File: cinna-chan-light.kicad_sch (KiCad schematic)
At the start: 0 parts

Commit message: first commit!!!
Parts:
- added U3: ESP32-S3-WROOM-1, RF_Module:ESP32-S3-WROOM-1, symbol RF_Module:ESP32-S3-WROOM-1
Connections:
- new net: U3.1 (GND), U3.40 (GND), U3.41 (GND)
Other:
- sheet usbcpd ports: added COM_I2C_SCL, COM_I2C_SDA; removed none
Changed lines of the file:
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@@
 	(wire
 		(pts
-			(xy 175.26 133.35) (xy 179.07 133.35)
+			(xy 180.34 133.35) (xy 175.26 133.35)
 		)
 		(stroke
@@
 			"Pn9vc9snPhAEQRAEADBoCkEQBEEQBEGQXQfdDARBEARBEARBdhl0MxAEQRAEQRAE2WX+AAB//OMf"
 			"97oYCIIgCIIgCILsH3A3A0EQBEEQBEGQXQbdDARBEARBEARBdhl0MxAEQRAEQRAE2WX+f6pzsk0v"
-			"m9qYAAAAAElFTkSuQmCC"
+			"m9qYAAAAAElFTkSuQmCCbQAoAEYAbwBvAHQAbgBvAHQAZQBBAHIAZQBhACkAIgA+AA0ADQAKADwA"
+			"ZQBsAGUAbQBlAG4AdAANAA0ACgBiAGEAYwBrAGcAcgBvAHUAbgBkACAAIAAgACAAIAAgACAAIAAg"
+			"ACAAPQAgACIAdABoAGUAbQBlAGEAYgBsAGUAKABkAHQAYgAoAFQAYQBzAGsARABpAGEAbABvAGcA"
+			"LAAgADEANQAsACAAMAApACwAIAB0AGgAcgBlAGUAZABmAGEAYwBlACkAIgANAA0ACgBwAGEAZABk"
+			"AGkAbgBnACAAIAAgACAAIAAgACAAIAAgACAAIAAgACAAPQAgACIAdABoAGUAbQBlAGEAYgBsAGUA"
+			"KABnAHQAbQBhAHIAKABUAGEAcwBrAEQAaQBhAGwAbwBnACwAIAAxADUALAAgADAALAAgADMANgAw"
+			"ADIAKQAsAHIAZQBjAHQAKAAxADAAcgBwACwAMAAsADEAMAByAHAALAAwACkAKQAiAA0ADQAKAC8A"
+			"PgANAA0ACgA8AC8AaQBmAD4ADQANAAoAPABpAGYAIABpAGQAPQAiAGEAdABvAG0AKABGAG8AbwB0"
+			"AG4AbwB0AGUASQBjAG8AbgApACIAPgANAA0ACgA8AGUAbABlAG0AZQBuAHQADQANAAoAaABlAGkA"
+			"ZwBoAHQAIAAgACAAIAAgACAAIAAgACAAIAAgACAAIAAgAD0AIAAiAHMAeQBzAG0AZQB0AHIAaQBj"
+			"ACgANAA5ACkAIgANAA0ACgB3AGkAZAB0AGgAIAAgACAAIAAgACAAIAAgACAAIAAgACAAIAAgACAA"
+			"PQAgACIAcwB5AHMAbQBlAHQAcgBpAGMAKAA1ADAAKQAiAA0ADQAKAGEAYwBjAGUAcwBzAGkAYgBs"
+			"AGUAIAAgACAAIAAgACAAIAAgACAAIAA9ACAAIgB0AHIAdQBlACIADQANAAoAYQBjAGMAcgBvAGwA"
+			"ZQAgACAAIAAgACAAIAAgACAAIAAgACAAIAAgAD0AIAAiAGcAcgBhAHAAaABpAGMAIgANAA0ACgAv"
+			"AD4ADQANAAoAPAAvAGkAZgA+AA0ADQAKADwAaQBmACAAaQBkAD0AIgBhAHQAbwBtACgARgBvAG8A"
+			"dABuAG8AdABlAFQAZQB4AHQAKQAiAD4ADQANAAoAPABlAGwAZQBtAGUAbgB0AA0ADQAKAGYAbwBu"
+			"AHQAIAAgACAAIAAgACAAIAAgACAAIAAgACAAIAAgACAAIAA9ACAAIgBnAHQAZgAoAFQAYQBzAGsA"
+			"RABpAGEAbABvAGcAUwB0AHkAbABlACwAIAAxADUALAAgADAAKQAiAA0ADQAKAGYAbwByAGUAZwBy"
+			"AG8AdQBuAGQAIAAgAA=="
 		)
 	)
@@
 		)
 	)
+	(symbol
+		(lib_id "RF_Module:ESP32-S3-WROOM-1")
+		(at 49.53 113.03 0)
+		(unit 1)
+		(exclude_from_sim no)
+		(in_bom yes)
+		(on_board yes)
+		(dnp no)
+		(fields_autoplaced yes)
+		(property "Reference" "U3"
+			(at 51.6733 82.55 0)
+			(effects
+				(font
+					(size 1.27 1.27)
+				)
+				(justify left)
+			)
+		)
+		(property "Value" "ESP32-S3-WROOM-1"
+			(at 51.6733 85.09 0)
+			(effects
+				(font
+					(size 1.27 1.27)
+				)
+				(justify left)
+			)
+		)
+		(property "Footprint" "RF_Module:ESP32-S3-WROOM-1"
+			(at 49.53 110.49 0)
+			(effects
+				(font
+					(size 1.27 1.27)
+				)
+				(hide yes)
+			)
+		)
+		(property "Datasheet" "https://www.espressif.com/sites/default/files/documentation/esp32-s3-wroom-1_wroom-1u_datasheet_en.pdf"
+			(at 49.53 113.03 0)
+			(effects
+				(font
+					(size 1.27 1.27)
+				)
+				(hide yes)
+			)
+		)
+		(property "Description" "RF Module, ESP32-S3 SoC, Wi-Fi 802.11b/g/n, Bluetooth, BLE, 32-bit, 3.3V, onboard antenna, SMD"
+			(at 49.53 113.03 0)
+			(effects
+				(font
+					(size 1.27 1.27)
+				)
+				(hide yes)
+			)
+		)
+		(pin "4"
+		)
+		(pin "25"
+		)
+		(pin "29"
+		)
+		(pin "41"
+		)
+		(pin "40"
+		)
+		(pin "28"
+		)
+		(pin "14"
+		)
+		(pin "15"
+		)
+		(pin "36"
+		)
+		(pin "2"
+		)
+		(pin "6"
+		)
+		(pin "7"
+		)
+		(pin "35"
+		)
+		(pin "26"
+		)
+		(pin "19"
+		)
+		(pin "20"
+		)
+		(pin "30"
+		)
+		(pin "27"
+		)
+		(pin "39"
+		)
+		(pin "5"
+		)
+		(pin "3"
+		)
+		(pin "8"
+		)
+		(pin "1"
+		)
+		(pin "23"
+		)
+		(pin "31"
+		)
+		(pin "24"
+		)
+		(pin "12"
+		)
+		(pin "10"
+		)
+		(pin "38"
+		)
+		(pin "18"
+		)
+		(pin "13"
+		)
+		(pin "32"
+		)
+		(pin "33"
+		)
+		(pin "34"
+		)
+		(pin "16"
+		)
+		(pin "9"
+		)
+		(pin "17"
+		)
+		(pin "22"
+		)
+		(pin "37"
+		)
+		(pin "21"
+		)
+		(pin "11"
+		)
+		(instances
+			(project ""
+				(path "/eccd34c1-1a5c-4187-bee1-b0d1b475f777"
+					(reference "U3")
+					(unit 1)
+				)
+			)
+		)
+	)
 	(sheet
-		(at 179.07 121.92)
-		(size 88.9 30.48)
+		(at 180.34 121.92)
+		(size 102.87 30.48)
 		(exclude_from_sim no)
 		(in_bom yes)
@@
 		)
 		(property "Sheetname" "usbcpd"
-			(at 179.07 121.2084 0)
+			(at 180.34 121.2084 0)
 			(effects
 				(font
@@
 		)
 		(property "Sheetfile" "usbcpd.kicad_sch"
-			(at 179.07 152.9846 0)
+			(at 180.34 152.9846 0)
 			(effects
 				(font
@@
 		)
 		(pin "PP_USBC_VBUS" input
-			(at 179.07 130.81 180)
+			(at 180.34 130.81 180)
 			(effects
 				(font
@@
 		)
 		(pin "PP_3V3_MAIN" input
-			(at 179.07 133.35 180)
+			(at 180.34 133.35 180)
 			(effects
 				(font
@@
 			)
 		)
+		(pin "COM_I2C_SCL" input
+			(at 180.34 128.27 180)
+			(effects
+				(font
+					(size 1.27 1.27)
+				)
+				(justify left)
+			)
+		)
+		(pin "COM_I2C_SDA" input
+			(at 204.47 121.92 90)
+			(effects
+				(font
+					(size 1.27 1.27)
+				)
+				(justify right)
+			)
+		)

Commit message: added lcsc, datasheet, and footprint. couldn't find zener and polarized stuff tho
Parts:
- U3: LCSC (none) -> C2913192
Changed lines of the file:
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@@
 			"AAAAAAAAAAAAAAAAAAAAAAAAAAAAAAAAAAAAAAAAAAAAAAAAAAAAAAAAAAAAAAAAAAAAAAAAAAAA"
 			"AAAAAAAAAAAAAAAAAAAAAAAAAAAAAAAAAAAAAAAAAAAAAAAAAAAAAAAAAAAAAAAAAAAAAAAAAAAA"
-			"AAAAAAAAAAAAAAAAAA=="
+			"AAAAAAAAAAAAAAAAAAAAAAAAAAAAAAAAAAAAAAAAAAAAAAAAAAAAAAAAAAAAAAAAAAAAAAAAAAAA"
+			"AAAAAAAAAAAAAAAAAAAAAAAAAAAAAAAAAAAAAAAAAAAAAAAAAAAAAAAAAAAAAAAAAAAAAAAAAAAA"
+			"AAAAAAAAAAAAAAAAAAAAAAAAAAAAAAAAAAAAAAAAAAAAAAAAAAAAAAAAAAAAAAAAAAAAAAAAAAAA"
+			"AAAAAAAAAAAAAAAAAAAAAAAAAAAAAAAAAAAAAAAAAAAAAAAAAAAAAAAAAAAAAAAAAAAAAAAAAAAA"
+			"AAAAAAAAAAAAAAAAAAAAAAAAAAAAAAAAAAAAAAAAAAAAAAAAAAAAAAAAAAAAAAAAAAAAAAAAAAAA"
+			"AAAAAAAAAAAAAAAAAAAAAAAAAAAAAAAAAAAAAAAAAAAAAAAAAAAAAAAAAAAAAAAAAAAAAAAAAAAA"
+			"AAAAAAAAAAAAAAAAAAAAAAAAAAAAAAAAAAAAAAAAAAAAAAAAAAAAAAAAAAAAAAAAAAAAAAAAAAAA"
+			"AAAAAAAAAAAAAAAAAAAAAAAAAAAAAAAAAAAAAAAAAAAAAAAAAAAAAAAAAAAAAAAAAAAAAAAAAAAA"
+			"AAAAAAAAAAAAAAAAAAAAAAAAAAAAAAAAAAAAAAAAAAAAAAAAAAAAAAAAAAAAAAAAAAAAAAAAAAAA"
+			"AAAAAAAAAAAAAAAAAAAAAAAAAAAAAAAAAAAAAAAAAAAAAAAAAAAAAAAAAAAAAAAAAAAAAAAAAAAA"
+			"AAAAAAAAAAAAAAAAAAAAAAAAAAAAAAAAAAAAAAAAAAAAAAAAAAAAAAAAAAAAAAAAAAAAAAAAAAAA"
+			"AAAAAAAAAAAAAAAAAAAAAAAAAAAAAAAAAAAAAAAAAAAAAAAAAAAAAAAAAAAAAAAAAAAAAAAAAAAA"
+			"AAAAAAAAAAAAAAAAAAAAAAAAAAAAAAAAAAAAAAAAAAAAAAAAAAAAAAAAAAAAAAAAAAAAAAAAAAAA"
+			"AAAAAAAAAAAAAAAAAAAAAAAAAAAAAAAAAAAAAAAAAAAAAAAAAAAAAAAAAAAAAAAAAAAAAAAAAAAA"
+			"AAAAAAAAAAAAAAAAAAAAAAAAAAAAAAAAAAAAAAAAAAAAAAAAAAAAAAAAAAAAAAAAAAAAAAAAAAAA"
+			"AAAAAAAAAAAAAAAAAAAAAAAAAAAAAAAAAAAAAAAAAAAAAAAAAAAAAAAAAAAAAAAAAAAAAAAAAAAA"
+			"AAAAAAAAAAAAAAAAAAAAAAAAAAAAAAAAAAAAAAAAAAAAAAAAAAAAAAAAAAAAAAAAAAAAAAAAAAAA"
+			"AAAAAAAAAAAAAAAAAAAAAAAAAAAAAAAAAAAAAAAAAAAAAAAAAAAAAAAAAAAAAAAAAAAAAAAAAAAA"
+			"AAAAAAAAAAAAAAAAAAAAAAAAAAAAAAAAAAAAAAAAAAAAAAAAAAAAAAAAAAAAAAAAAAAAAAAAAAAA"
+			"AAAAAAAAAAAAAAAAAAAAAAAAAAAAAAAAAAAAAAAAAAAAAAAAAAAAAAAAAAAAAAAAAAAAAAAAAAAA"
+			"AAAAAAAAAAAAAAAAAAAAAAAAAAAAAAAAAAAAAAAAAAAAAAAAAAAAAAAAAAAAAAAAAAAAAAAAAAAA"
+			"AAAAAAAAAAAAAAAAAAAAAAAAAAAAAAAAAAAAAAAAAAAAAAAAAAAAAAAAAAAAAAAAAAAAAAAAAAAA"
+			"AAAAAAAAAAAAAAAAAAAAAAAAAAAAAAAAAAAAAAAAAAAAAAAAAAAAAAAAAAAAAAAAAAAAAAAAAAAA"
+			"AAAAAAAAAAAAAAAAAAAAAAAAAAAAAAAAAAAAAAAAAAAAAAAAAAAAAAAAAAAAAAAAAAAAAAAAAAAA"
+			"AAAAAAAAAAAAAAAAAAAAAAAAAAAAAAAAAAAAAAAAAAAAAAAAAAAAAAAAAAAAAAAAAAAAAAAAAAAA"
+			"AAAAAAAAAAAAAAAAAAAAAAAAAAAAAAAAAAAAAAAAAAAAAAAAAAAAAAAAAAAAAAAAAAAAAAAAAAAA"
+			"AAAAAAAAAAAAAAAAAAAAAAAAAAAAAAAAAAAAAAAAAAAAAAAAAAAAAAAAAAAAAAAAAAAAAAAAAAAA"
+			"AAAAAAAAAAAAAAAAAAAAAAAAAAAAAAAAAAAAAAAAAAAAAAAAAAAAAAAAAAAAAAAAAAAAAAAAAAAA"
+			"AAAAAAAAAAAAAAAAAAAAAAAAAAAAAAAAAAAAAAAAAAAAAAAAAAAAAAAAAAAAAAAAAAAAAAAAAAAA"
+			"AAAAAAAAAAAAAAAAAAAAAAAAAAAAAAAAAAAAAAAAAAAAAAAAAAAAAAAAAAAAAAAAAAAAAAAAAAAA"
+			"AAAAAAAAAAAAAAAAAAAAAAAAAAAAAAAAAAAAAAAAAAAAAAAAAAAAAAAAAAAAAAAAAAAAAAAAAAAA"
+			"AAAAAAAAAAAAAAAAAAAAAAAAAAAAAAAAAAAAAAAAAAAAAAAAAAAAAAAAAAAAAAAAAAAAAAAAAAAA"
+			"AAAAAAAAAAAAAAAAAAAAAAAAAAAAAAAAAAAAAAAAAAAAAAAAAAAAAAAAAAAAAAAAAAAAAAAAAAAA"
+			"AAAAAAAAAAAAAAAAAADlr2hYAAQAgPj/////////AMM4B+IBAAD4/////////wDnOAfiAQAA+P//"
+			"//////8AwTgH4gEAAPj/////////wOU4B+IBAAD4/////////8DqOAfiAQAA+P////////+AxDgH"
+			"4gEAAPj/////////ALg4B+IBAAD4/////////wDuOAfiAQAA+P////////+A8jgH4gEAAPj/////"
+			"////gME4B+IBAAD4/w=="
 		)
 	)
@@
 			(at 49.53 113.03 0)
 			(effects
+				(font
+					(size 1.27 1.27)
+				)
+				(hide yes)
+			)
+		)
+		(property "LCSC" "C2913192"
+			(at 49.53 113.03 0)
+			(effects

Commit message: Add light-white
Signed-off-by: sanyue <sanyue7th@gmail.com>
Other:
- added sheet light_white (light_white.kicad_sch)
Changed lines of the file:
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@@
 			"//////8AwTgH4gEAAPj/////////wOU4B+IBAAD4/////////8DqOAfiAQAA+P////////+AxDgH"
 			"4gEAAPj/////////ALg4B+IBAAD4/////////wDuOAfiAQAA+P////////+A8jgH4gEAAPj/////"
-			"////gME4B+IBAAD4/w=="
+			"////gME4B+IBAAD4/wAAAAAAAAAAAAAAAAAAAAAAAAAAAAAAAAAAAAAAAAAAAAAAAAAAAAAAAAAA"
+			"AAAAAAAAAAAAAAAAAAAAAAAAAAAAAAAAAAAAAAAAAAAAAAAAAAAAAAAAAAAAAAAAAAAAAAAAAAAA"
+			"AAAAAAAAAAAAAAAAAAAAAAAAAAAAAAAAAAAAAAAAAAAAAAAAAAAAAAAAAAAAAAAAAAAAAAAAAAAA"
+			"AAAAAAAAAAAAAAAAAAAAAAAAAAAAAAAAAAAAAAAAAAAAAAAAAAAAAAAAAAAAAAAAAAAAAAAAAAAA"
+			"AAAAAAAAAAAAAAAAAAAAAAAAAAAAAAAAAAAAAAAAAAAAAAAAAAAAAAAAAAAAAAAAAAAAAAAAAAAA"
+			"AAAAAAAAAAAAAAAAAAAAAAAAAAAAAAAAAAAAAAAAAAAAAAAAAAAAAAAAAAAAAAAAAAAAAAAAAAAA"
+			"AAAAAAAAAAAAAAAAAAAAAAAAAAAAAAAAAAAAAAAAAAAAAAAAAAAAAAAAAAAAAAAAAAAAAAAAAAAA"
+			"AAAAAAAAAAAAAAAAAAAAAAAAAAAAAAAAAAAAAAAAAAAAAAAAAAAAAAAAAAAAAAAAAAAAAAAAAAAA"
+			"AAAAAAAAAAAAAAAAAAAAAAAAAAAAAAAAAAAAAAAAAAAAAAAAAAAAAAAAAAAAAAAAAAAAAAAAAAAA"
+			"AAAAAAAAAAAAAAAAAAAAAAAAAAAAAAAAAAAAAAAAAAAAAAAAAAAAAAAAAAAAAAAAAAAAAAAAAAAA"
+			"AAAAAAAAAAAAAAAAAAAAAAAAAAAAAAAAAAAAAAAAAAAAAAAAAAAAAAAAAAAAAAAAAAAAAAAAAAAA"
+			"AAAAAAAAAAAAAAAAAAAAAAAAAAAAAAAAAAAAAAAAAAAAAAAAAAAAAAAAAAAAAAAAAAAAAAAAAAAA"
+			"AAAAAAAAAAAAAAAAAAAAAAAAAAAAAAAAAAAAAAAAAAAAAAAAAAAAAAAAAAAAAAAAAAAAAAAAAAAA"
+			"AAAAAAAAAAAAAAAAAAAAAAAAAAAAAAAAAAAAAAAAAAAAAAAAAAAAAAAAAAAAAAAAAAAAAAAAAAAA"
+			"AAAAAAAAAAAAAAAAAAAAAAAAAAAAAAAAAAAAAAAAAAAAAAAAAAAAAAAAAAAAAAAAAAAAAAAAAAAA"
+			"AAAAAAAAAAAAAAAAAAAAAAAAAAAAAAAAAAAAAAAAAAAAAAAAAAAAAAAAAAAAAAAAAAAAAAAAAAAA"
+			"AAAAAAAAAAAAAAAAAAAAAAAAAAAAAAAAAAAAAAAAAAAAAAAAAAAAAAAAAAAAAAAAAAAAAAAAAAAA"
+			"AAAAAAAAAAAAAAAAAAAAAAAAAAAAAAAAAAAAAAAAAAAAAAAAAAAAAAAAAAAAAAAAAAAAAAAAAAAA"
+			"AAAAAAAAAAAAAAAAAA=="
 		)
 	)
@@
 				)
 			)
+		)
+	)
+	(sheet
+		(at 157.48 33.02)
+		(size 81.28 20.32)
+		(exclude_from_sim no)
+		(in_bom yes)
+		(on_board yes)
+		(dnp no)
+		(fields_autoplaced yes)
+		(stroke
+			(width 0.1524)
+			(type solid)
+		)
+		(fill
+			(color 0 0 0 0.0000)
+		)
+		(property "Sheetname" "light_white"
+			(at 157.48 32.3084 0)
+			(effects
+				(font
+					(size 1.27 1.27)
+				)
+				(justify left bottom)
+			)
+		)
+		(property "Sheetfile" "light_white.kicad_sch"
+			(at 157.48 53.9246 0)
+			(effects
+				(font
+					(size 1.27 1.27)
+				)
+				(justify left top)
+			)
+		)
+		(instances
+			(project "cinna-chan-light"
+				(path "/eccd34c1-1a5c-4187-bee1-b0d1b475f777"
+					(page "4")
+				)
+			)

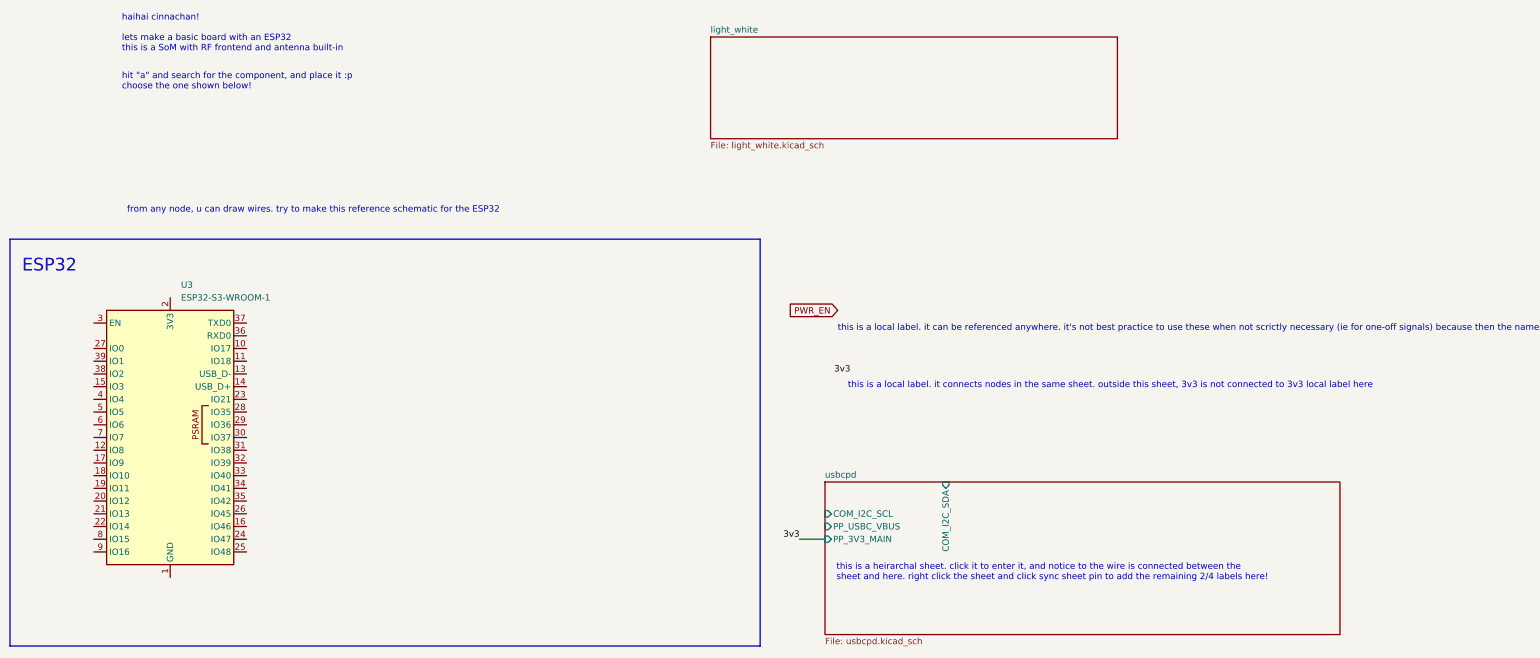
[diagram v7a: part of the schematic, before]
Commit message: Cleanup, add 5vREG block
Signed-off-by: sanyue <sanyue7th@gmail.com>
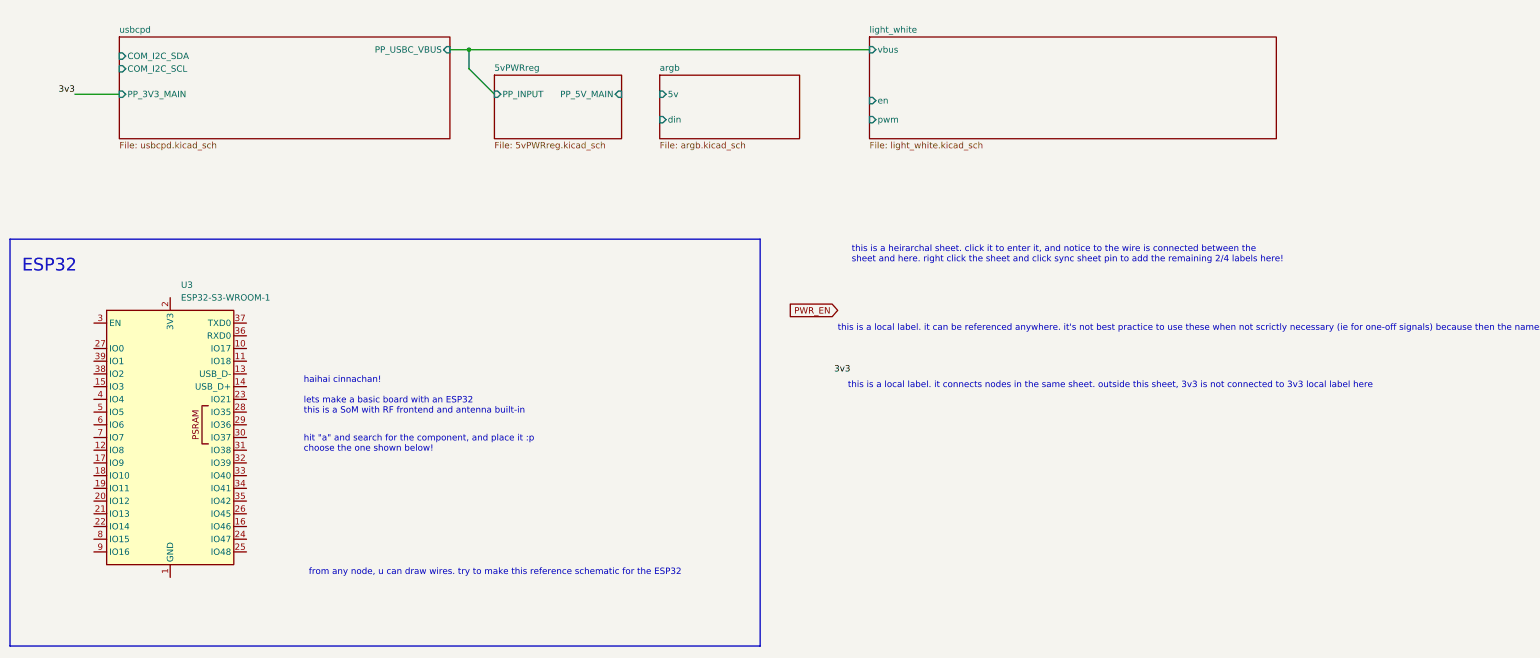
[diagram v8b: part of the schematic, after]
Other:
- added sheet 5vPWRreg (5vPWRreg.kicad_sch)
- added sheet argb (argb.kicad_sch)
- sheet light_white ports: added en, pwm, vbus; removed none
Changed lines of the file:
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@@
 	(text "haihai cinnachan!\n\nlets make a basic board with an ESP32\nthis is a SoM with RF frontend and antenna built-in"
 		(exclude_from_sim no)
-		(at 39.878 32.258 0)
+		(at 76.2 104.648 0)
 		(effects
 			(font
@@
 	(text "hit \"a\" and search for the component, and place it :p\nchoose the one shown below!"
 		(exclude_from_sim no)
-		(at 39.878 41.91 0)
+		(at 76.2 114.3 0)
 		(effects
 			(font
@@
 	(text "this is a heirarchal sheet. click it to enter it, and notice to the wire is connected between the \nsheet and here. right click the sheet and click sync sheet pin to add the remaining 2/4 labels here!"
 		(exclude_from_sim no)
-		(at 182.626 139.954 0)
+		(at 185.674 76.454 0)
 		(effects
 			(font
@@
 	(text "from any node, u can draw wires. try to make this reference schematic for the ESP32"
 		(exclude_from_sim no)
-		(at 40.894 67.564 0)
+		(at 77.216 139.954 0)
 		(effects
 			(font
@@
 		)
 	)
+	(junction
+		(at 109.22 35.56)
+		(diameter 0)
+		(color 0 0 0 0)
+	)
 	(wire
 		(pts
-			(xy 180.34 133.35) (xy 175.26 133.35)
+			(xy 109.22 35.56) (xy 189.23 35.56)
 		)
 		(stroke
@@
 		)
 	)
+	(wire
+		(pts
+			(xy 105.41 35.56) (xy 109.22 35.56)
+		)
+		(stroke
+			(width 0)
+			(type default)
+		)
+	)
+	(wire
+		(pts
+			(xy 109.22 39.37) (xy 114.3 44.45)
+		)
+		(stroke
+			(width 0)
+			(type default)
+		)
+	)
+	(wire
+		(pts
+			(xy 39.37 44.45) (xy 30.48 44.45)
+		)
+		(stroke
+			(width 0)
+			(type default)
+		)
+	)
+	(wire
+		(pts
+			(xy 109.22 39.37) (xy 109.22 35.56)
+		)
+		(stroke
+			(width 0)
+			(type default)
+		)
+	)
 	(image
-		(at 63.5 53.34)
+		(at 99.822 125.73)
 		(scale 0.160512)
 		(data "iVBORw0KGgoAAAANSUhEUgAABCIAAAGQCAIAAAD0iVbdAAAAA3NCSVQICAjb4U/gAAAACXBIWXMA"
@@
 			"AAAAAAAAAAAAAAAAAAAAAAAAAAAAAAAAAAAAAAAAAAAAAAAAAAAAAAAAAAAAAAAAAAAAAAAAAAAA"
 			"AAAAAAAAAAAAAAAAAAAAAAAAAAAAAAAAAAAAAAAAAAAAAAAAAAAAAAAAAAAAAAAAAAAAAAAAAAAA"
+			"AAAAAAAAAAAAAAAAAAAAAAAAAAAAAAAAAAAAAAAAAAAAAAAAAAAAAAAAAAAAAAAAAAAAAAAAAAAA"
+			"AAAAAAAAAAAAAAAAAAAAAAAAAAAAAAAAAAAAAAAAAAAAAAAAAAAAAAAAAAAAAAAAAAAAAAAAAAAA"
+			"AAAAAAAAAAAAAAAAAAAAAAAAAAAAAAAAAAAAAAAAAAAAAAAAAAAAAAAAAAAAAAAAAAAAAAAAAAAA"
+			"AAAAAAAAAAAAAAAAAAAAAAAAAAAAAAAAAAAAAAAAAAAAAAAAAAAAAAAAAAAAAAAAAAAAAAAAAAAA"
+			"AAAAAAAAAAAAAAAAAAAAAAAAAAAAAAAAAAAAAAAAAAAAAAAAAAAAAAAAAAAAAAAAAAAAAAAAAAAA"
+			"AAAAAAAAAAAAAAAAAAAAAAAAAAAAAAAAAAAAAAAAAAAAAAAAAAAAAAAAAAAAAAAAAAAAAAAAAAAA"
+			"AAAAAAAAAAAAAAAAAAAAAAAAAAAAAAAAAAAAAAAAAAAAAAAAAAAAAAAAAAAAAAAAAAAAAAAAAAAA"
+			"AAAAAAAAAAAAAAAAAAAAAAAAAAAAAAAAAAAAAAAAAAAAAAAAAAAAAAAAAAAAAAAAAAAAAAAAAAAA"
+			"AAAAAAAAAAAAAAAAAAAAAAAAAAAAAAAAAAAAAAAAAAAAAAAAAAAAAAAAAAAAAAAAAAAAAAAAAAAA"
+			"AAAAAAAAAAAAAAAAAAAAAAAAAAAAAAAAAAAAAAAAAAAAAAAAAAAAAAAAAAAAAAAAAAAAAAAAAAAA"
+			"AAAAAAAAAAAAAAAAAAAAAAAAAAAAAAAAAAAAAAAAAAAAAAAAAAAAAAAAAAAAAAAAAAAAAAAAAAAA"
+			"AAAAAAAAAAAAAAAAAAAAAAAAAAAAAAAAAAAAAAAAAAAAAAAAAAAAAAAAAAAAAAAAAAAAAAAAAAAA"
+			"AAAAAAAAAAAAAAAAAAAAAAAAAAAAAAAAAAAAAAAAAAAAAAAAAAAAAAAAAAAAAAAAAAAAAAAAAAAA"
+			"AAAAAAAAAAAAAAAAAAAAAAAAAAAAAAAAAAAAAAAAAAAAAAAAAAAAAAAAAAAAAAAAAAAAAAAAAAAA"
+			"AAAAAAAAAAAAAAAAAAAAAAAAAAAAAAAAAAAAAAAAAAAAAAAAAAAAAAAAAAAAAAAAAAAAAAAAAAAA"
+			"AAAAAAAAAAAAAAAAAAAAAAAAAAAAAAAAAAAAAAAAAAAAAAAAAAAAAAAAAAAAAAAAAAAAAAAAAAAA"
+			"AAAAAAAAAAAAAAAAAAAAAAAAAAAAAAAAAAAAAAAAAAAAAAAAAAAAAAAAAAAAAAAAAAAAAAAAAAAA"
+			"AAAAAAAAAAAAAAAAAAAAAAAAAAAAAAAAAAAAAAAAAAAAAAAAAAAAAAAAAAAAAAAAAAAAAAAAAAAA"
 			"AAAAAAAAAAAAAAAAAA=="
 		)
 	)
 	(label "3v3"
-		(at 175.26 133.35 180)
+		(at 30.48 44.45 180)
 		(effects
 			(font
@@
 	)
 	(sheet
-		(at 157.48 33.02)
+		(at 114.3 40.64)
+		(size 25.4 12.7)
+		(exclude_from_sim no)
+		(in_bom yes)
+		(on_board yes)
+		(dnp no)
+		(fields_autoplaced yes)
+		(stroke
+			(width 0.1524)
+			(type solid)
+		)
+		(fill
+			(color 0 0 0 0.0000)
+		)
+		(property "Sheetname" "5vPWRreg"
+			(at 114.3 39.9284 0)
+			(effects
+				(font
+					(size 1.27 1.27)
+				)
+				(justify left bottom)
+			)
+		)
+		(property "Sheetfile" "5vPWRreg.kicad_sch"
+			(at 114.3 53.9246 0)
+			(effects
+				(font
+					(size 1.27 1.27)
+				)
+				(justify left top)
+			)
+		)
+		(pin "PP_INPUT" input
+			(at 114.3 44.45 180)
+			(effects
+				(font
+					(size 1.27 1.27)
+				)
+				(justify left)
+			)
+		)
+		(pin "PP_5V_MAIN" input
+			(at 139.7 44.45 0)
+			(effects
+				(font
+					(size 1.27 1.27)
+				)
+				(justify right)
+			)
+		)
+		(instances
+			(project "cinna-chan-light"
+				(path "/eccd34c1-1a5c-4187-bee1-b0d1b475f777"
+					(page "5")
+				)
+			)
+		)
+	)
+	(sheet
+		(at 189.23 33.02)
 		(size 81.28 20.32)
 		(exclude_from_sim no)
@@
 		)
 		(property "Sheetname" "light_white"
-			(at 157.48 32.3084 0)
+			(at 189.23 32.3084 0)
 			(effects
 				(font
@@
 		)
 		(property "Sheetfile" "light_white.kicad_sch"
-			(at 157.48 53.9246 0)
+			(at 189.23 53.9246 0)
 			(effects
 				(font
@@
 				)
 				(justify left top)
+			)
+		)
+		(pin "en" input
+			(at 189.23 45.72 180)
+			(effects
+				(font
+					(size 1.27 1.27)
+				)
+				(justify left)
+			)
+		)
+		(pin "vbus" input
+			(at 189.23 35.56 180)
+			(effects
+				(font
+					(size 1.27 1.27)
+				)
+				(justify left)
+			)
+		)
+		(pin "pwm" input
+			(at 189.23 49.53 180)
+			(effects
+				(font
+					(size 1.27 1.27)
+				)
+				(justify left)
 			)
 		)
@@
 	)
 	(sheet
-		(at 180.34 121.92)
-		(size 102.87 30.48)
+		(at 147.32 40.64)
+		(size 27.94 12.7)
 		(exclude_from_sim no)
 		(in_bom yes)
@@
 			(color 0 0 0 0.0000)
 		)
+		(property "Sheetname" "argb"
+			(at 147.32 39.9284 0)
+			(effects
+				(font
+					(size 1.27 1.27)
+				)
+				(justify left bottom)
+			)
+		)
+		(property "Sheetfile" "argb.kicad_sch"
+			(at 147.32 53.9246 0)
+			(effects
+				(font
+					(size 1.27 1.27)
+				)
+				(justify left top)
+			)
+		)
+		(pin "din" input
+			(at 147.32 49.53 180)
+			(effects
+				(font
+					(size 1.27 1.27)
+				)
+				(justify left)
+			)
+		)
+		(pin "5v" input
+			(at 147.32 44.45 180)
+			(effects
+				(font
+					(size 1.27 1.27)
+				)
+				(justify left)
+			)
+		)
+		(instances
+			(project "cinna-chan-light"
+				(path "/eccd34c1-1a5c-4187-bee1-b0d1b475f777"
+					(page "6")
+				)
+			)
+		)
+	)
+	(sheet
+		(at 39.37 33.02)
+		(size 66.04 20.32)
+		(exclude_from_sim no)
+		(in_bom yes)
+		(on_board yes)
+		(dnp no)
+		(fields_autoplaced yes)
+		(stroke
+			(width 0.1524)
+			(type solid)
+		)
+		(fill
+			(color 0 0 0 0.0000)
+		)
 		(property "Sheetname" "usbcpd"
-			(at 180.34 121.2084 0)
+			(at 39.37 32.3084 0)
 			(effects
 				(font
@@
 		)
 		(property "Sheetfile" "usbcpd.kicad_sch"
-			(at 180.34 152.9846 0)
+			(at 39.37 53.9246 0)
 			(effects
 				(font
@@
 		)
 		(pin "PP_USBC_VBUS" input
-			(at 180.34 130.81 180)
+			(at 105.41 35.56 0)
+			(effects
+				(font
+					(size 1.27 1.27)
+				)
+				(justify right)
+			)
+		)
+		(pin "PP_3V3_MAIN" input
+			(at 39.37 44.45 180)
 			(effects
 				(font
@@
 			)
 		)
-		(pin "PP_3V3_MAIN" input
-			(at 180.34 133.35 180)
+		(pin "COM_I2C_SCL" input
+			(at 39.37 39.37 180)
 			(effects
 				(font
@@
 			)
 		)
-		(pin "COM_I2C_SCL" input
-			(at 180.34 128.27 180)
+		(pin "COM_I2C_SDA" input
+			(at 39.37 36.83 180)
 			(effects
 				(font
@@
 			)
 		)
-		(pin "COM_I2C_SDA" input
-			(at 204.47 121.92 90)
-			(effects
-				(font
-					(size 1.27 1.27)
-				)
-				(justify right)
-			)
-		)
